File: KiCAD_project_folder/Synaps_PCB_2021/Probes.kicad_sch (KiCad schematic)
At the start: 2 parts, among them J3 Conn_01x20_MountingPin, U2 CD74HC4067M

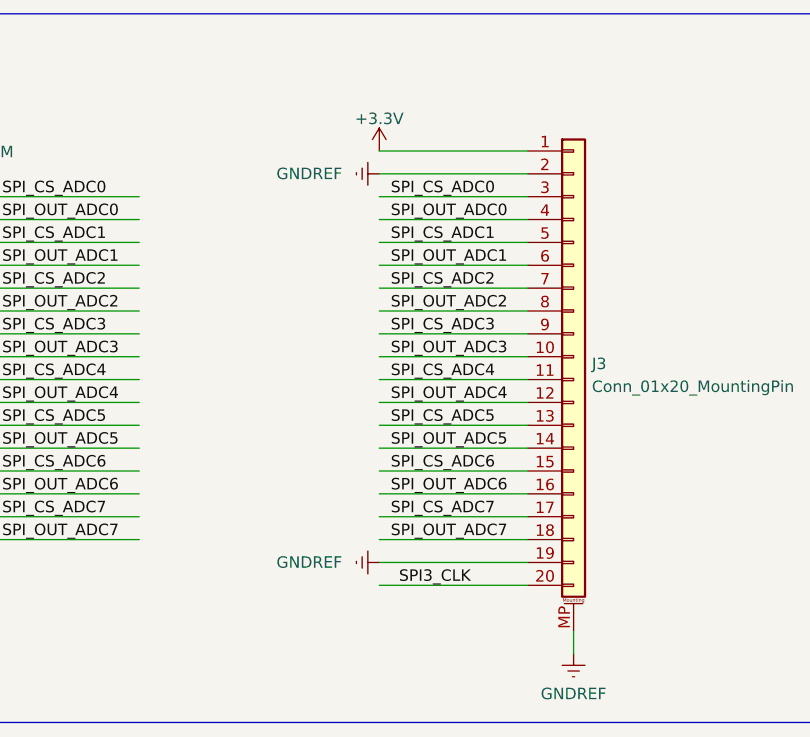
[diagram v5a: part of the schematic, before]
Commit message: Fixed missing connections + plus added rough BOM
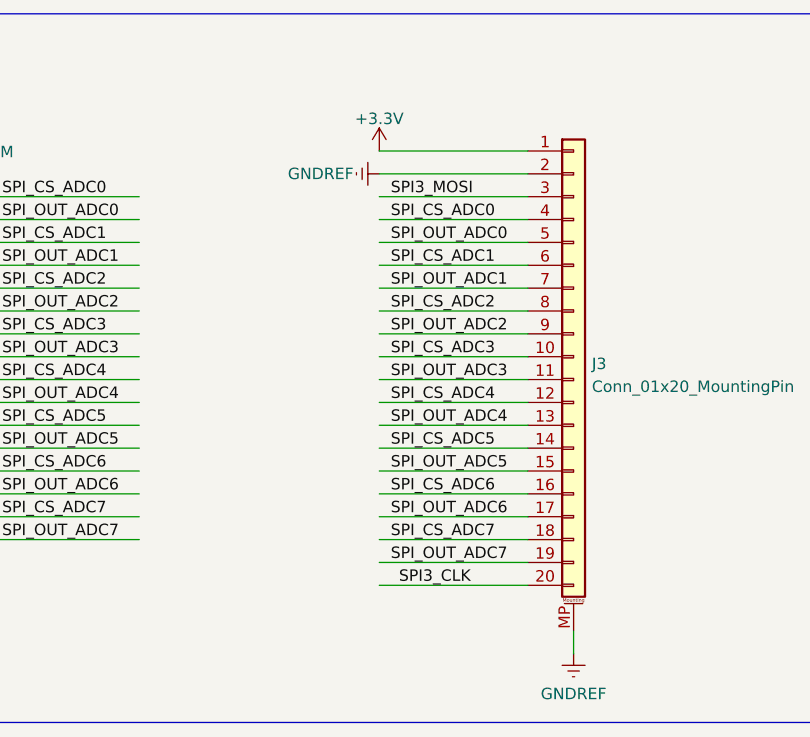
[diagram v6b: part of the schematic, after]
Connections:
- net GNDREF: no longer J3.19 (Pin_19)
- net SPI3_MOSI: now also J3.3 (Pin_3)
- net SPI_CS_ADC0: now also J3.4 (Pin_4); no longer J3.3 (Pin_3)
- net SPI_CS_ADC1: now also J3.6 (Pin_6); no longer J3.5 (Pin_5)
- net SPI_CS_ADC2: now also J3.8 (Pin_8); no longer J3.7 (Pin_7)
- net SPI_CS_ADC3: now also J3.10 (Pin_10); no longer J3.9 (Pin_9)
- net SPI_CS_ADC4: now also J3.12 (Pin_12); no longer J3.11 (Pin_11)
- net SPI_CS_ADC5: now also J3.14 (Pin_14); no longer J3.13 (Pin_13)
- net SPI_CS_ADC6: now also J3.16 (Pin_16); no longer J3.15 (Pin_15)
- net SPI_CS_ADC7: now also J3.18 (Pin_18); no longer J3.17 (Pin_17)
- net SPI_OUT_ADC0: now also J3.5 (Pin_5); no longer J3.4 (Pin_4)
- net SPI_OUT_ADC1: now also J3.7 (Pin_7); no longer J3.6 (Pin_6)
- net SPI_OUT_ADC2: now also J3.9 (Pin_9); no longer J3.8 (Pin_8)
- net SPI_OUT_ADC3: now also J3.11 (Pin_11); no longer J3.10 (Pin_10)
- net SPI_OUT_ADC4: now also J3.13 (Pin_13); no longer J3.12 (Pin_12)
- net SPI_OUT_ADC5: now also J3.15 (Pin_15); no longer J3.14 (Pin_14)
- net SPI_OUT_ADC6: now also J3.17 (Pin_17); no longer J3.16 (Pin_16)
- net SPI_OUT_ADC7: now also J3.19 (Pin_19); no longer J3.18 (Pin_18)
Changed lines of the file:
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@@
     (effects (font (size 1.27 1.27)) (justify left bottom))
   )
-  (label "SPI_OUT_ADC7" (at 199.39 81.28 0)
-    (effects (font (size 1.27 1.27)) (justify left bottom))
-  )
-  (label "SPI_CS_ADC7" (at 199.39 78.74 0)
+  (label "SPI_OUT_ADC7" (at 199.39 83.82 0)
+    (effects (font (size 1.27 1.27)) (justify left bottom))
+  )
+  (label "SPI_CS_ADC7" (at 199.39 81.28 0)
     (effects (font (size 1.27 1.27)) (justify left bottom))
   )
@@
     (effects (font (size 1.27 1.27)) (justify left bottom))
   )
-  (label "SPI_OUT_ADC2" (at 199.39 55.88 0)
-    (effects (font (size 1.27 1.27)) (justify left bottom))
-  )
-  (label "SPI_OUT_ADC3" (at 199.39 60.96 0)
-    (effects (font (size 1.27 1.27)) (justify left bottom))
-  )
-  (label "SPI_CS_ADC6" (at 199.39 73.66 0)
+  (label "SPI3_MOSI" (at 199.39 43.18 0)
+    (effects (font (size 1.27 1.27)) (justify left bottom))
+  )
+  (label "SPI_OUT_ADC2" (at 199.39 58.42 0)
+    (effects (font (size 1.27 1.27)) (justify left bottom))
+  )
+  (label "SPI_OUT_ADC3" (at 199.39 63.5 0)
+    (effects (font (size 1.27 1.27)) (justify left bottom))
+  )
+  (label "SPI_CS_ADC6" (at 199.39 76.2 0)
     (effects (font (size 1.27 1.27)) (justify left bottom))
   )
@@
     (effects (font (size 1.27 1.27)) (justify right bottom))
   )
-  (label "SPI_CS_ADC3" (at 199.39 58.42 0)
+  (label "SPI_CS_ADC3" (at 199.39 60.96 0)
     (effects (font (size 1.27 1.27)) (justify left bottom))
   )
@@
     (effects (font (size 1.27 1.27)) (justify left bottom))
   )
-  (label "SPI_CS_ADC4" (at 199.39 63.5 0)
+  (label "SPI_CS_ADC4" (at 199.39 66.04 0)
     (effects (font (size 1.27 1.27)) (justify left bottom))
   )
@@
     (effects (font (size 1.27 1.27)) (justify left bottom))
   )
-  (label "SPI_CS_ADC0" (at 199.39 43.18 0)
-    (effects (font (size 1.27 1.27)) (justify left bottom))
-  )
-  (label "SPI_OUT_ADC0" (at 199.39 45.72 0)
-    (effects (font (size 1.27 1.27)) (justify left bottom))
-  )
-  (label "SPI_CS_ADC1" (at 199.39 48.26 0)
-    (effects (font (size 1.27 1.27)) (justify left bottom))
-  )
-  (label "SPI_CS_ADC2" (at 199.39 53.34 0)
-    (effects (font (size 1.27 1.27)) (justify left bottom))
-  )
-  (label "SPI_CS_ADC5" (at 199.39 68.58 0)
+  (label "SPI_CS_ADC0" (at 199.39 45.72 0)
+    (effects (font (size 1.27 1.27)) (justify left bottom))
+  )
+  (label "SPI_OUT_ADC0" (at 199.39 48.26 0)
+    (effects (font (size 1.27 1.27)) (justify left bottom))
+  )
+  (label "SPI_CS_ADC1" (at 199.39 50.8 0)
+    (effects (font (size 1.27 1.27)) (justify left bottom))
+  )
+  (label "SPI_CS_ADC2" (at 199.39 55.88 0)
+    (effects (font (size 1.27 1.27)) (justify left bottom))
+  )
+  (label "SPI_CS_ADC5" (at 199.39 71.12 0)
     (effects (font (size 1.27 1.27)) (justify left bottom))
   )
@@
     (effects (font (size 1.27 1.27)) (justify right bottom))
   )
-  (label "SPI_OUT_ADC6" (at 199.39 76.2 0)
-    (effects (font (size 1.27 1.27)) (justify left bottom))
-  )
-  (label "SPI_OUT_ADC1" (at 199.39 50.8 0)
-    (effects (font (size 1.27 1.27)) (justify left bottom))
-  )
-  (label "SPI_OUT_ADC5" (at 199.39 71.12 0)
+  (label "SPI_OUT_ADC6" (at 199.39 78.74 0)
+    (effects (font (size 1.27 1.27)) (justify left bottom))
+  )
+  (label "SPI_OUT_ADC1" (at 199.39 53.34 0)
+    (effects (font (size 1.27 1.27)) (justify left bottom))
+  )
+  (label "SPI_OUT_ADC5" (at 199.39 73.66 0)
     (effects (font (size 1.27 1.27)) (justify left bottom))
   )
@@
     (effects (font (size 1.27 1.27)) (justify right bottom))
   )
-  (label "SPI_OUT_ADC4" (at 199.39 66.04 0)
+  (label "SPI_OUT_ADC4" (at 199.39 68.58 0)
     (effects (font (size 1.27 1.27)) (justify left bottom))
   )
@@
     (pin "MP")
   )
+  (symbol (lib_id "power:GNDREF") (at 198.12 40.64 270) (unit 1)
+    (in_bom yes) (on_board yes)
+    (property "Reference" "#PWR0101" (id 0) (at 191.77 40.64 0)
+      (effects (font (size 1.27 1.27)) hide)
+    )
+    (property "Value" "GNDREF" (id 1) (at 187.96 40.64 90)
+      (effects (font (size 1.27 1.27)) (justify left))
+    )
+    (property "Footprint" "" (id 2) (at 198.12 40.64 0)
+      (effects (font (size 1.27 1.27)) hide)
+    )
+    (property "Datasheet" "" (id 3) (at 198.12 40.64 0)
+      (effects (font (size 1.27 1.27)) hide)
+    )
+    (pin "1")
+  )
   (symbol (lib_id "power:+3.3V") (at 198.12 38.1 0) (unit 1)
     (in_bom yes) (on_board yes) (fields_autoplaced)
@@
       (effects (font (size 1.27 1.27)) hide)
     )
-    (pin "1")
-  )
-  (symbol (lib_id "power:GNDREF") (at 198.12 83.82 270) (unit 1)
-    (in_bom yes) (on_board yes)
-    (property "Reference" "#PWR050" (id 0) (at 191.77 83.82 0)
-      (effects (font (size 1.27 1.27)) hide)
-    )
-    (property "Value" "GNDREF" (id 1) (at 186.69 83.82 90)
-      (effects (font (size 1.27 1.27)) (justify left))
-    )
-    (property "Footprint" "" (id 2) (at 198.12 83.82 0)
-      (effects (font (size 1.27 1.27)) hide)
-    )
-    (property "Datasheet" "" (id 3) (at 198.12 83.82 0)
-      (effects (font (size 1.27 1.27)) hide)
-    )
-    (pin "1")
-  )
-  (symbol (lib_id "power:GNDREF") (at 198.12 40.64 270) (unit 1)
-    (in_bom yes) (on_board yes)
-    (property "Reference" "#PWR049" (id 0) (at 191.77 40.64 0)
-      (effects (font (size 1.27 1.27)) hide)
-    )
-    (property "Value" "GNDREF" (id 1) (at 186.69 40.64 90)
-      (effects (font (size 1.27 1.27)) (justify left))
-    )
-    (property "Footprint" "" (id 2) (at 198.12 40.64 0)
-      (effects (font (size 1.27 1.27)) hide)
-    )
-    (property "Datasheet" "" (id 3) (at 198.12 40.64 0)
-      (effects (font (size 1.27 1.27)) hide)
-    )

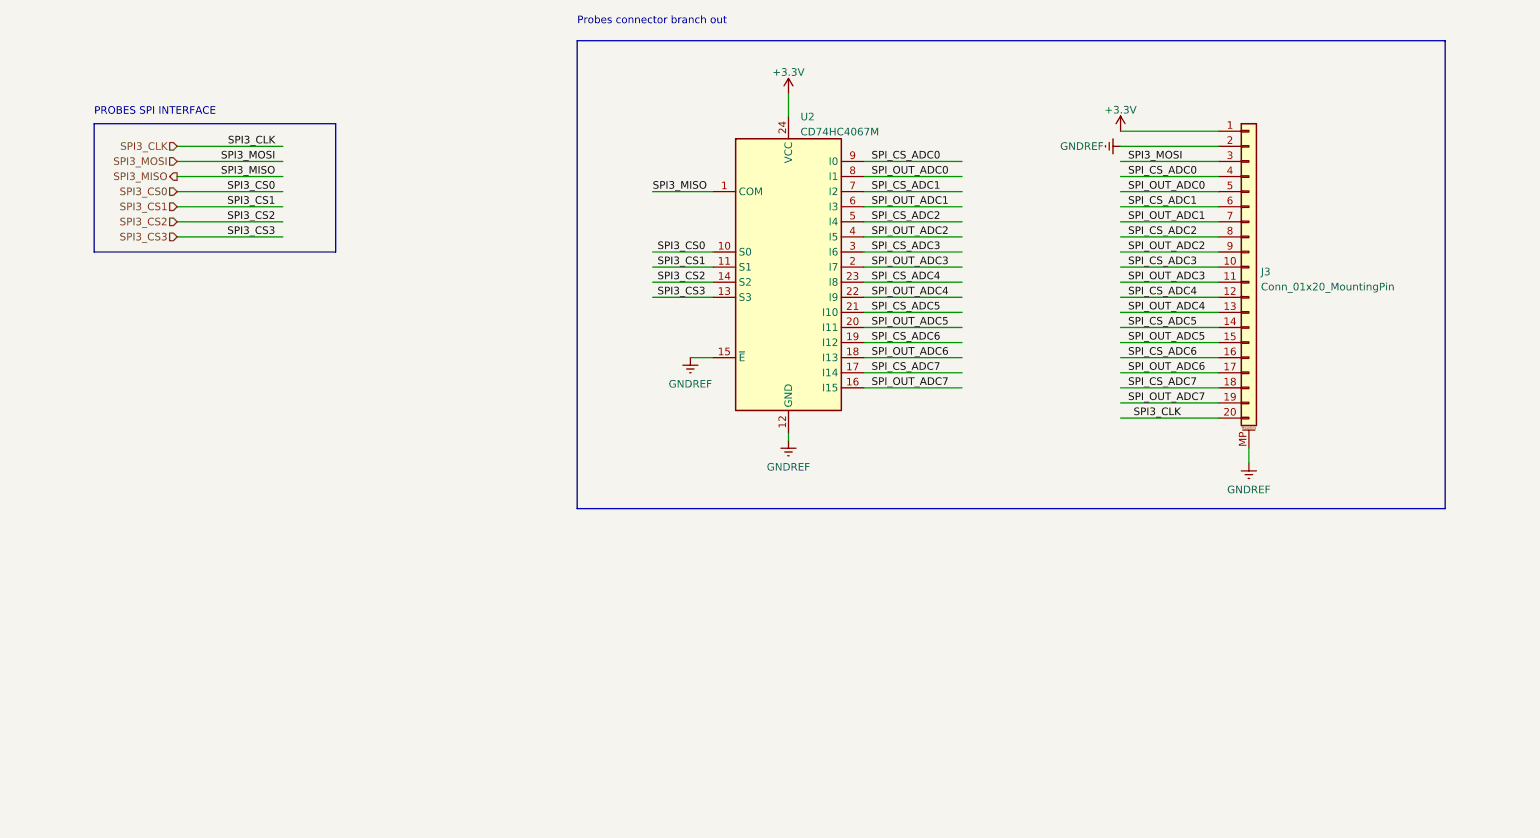
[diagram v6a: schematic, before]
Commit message: Updated BOM and power circuit has to be redone because of missing parts
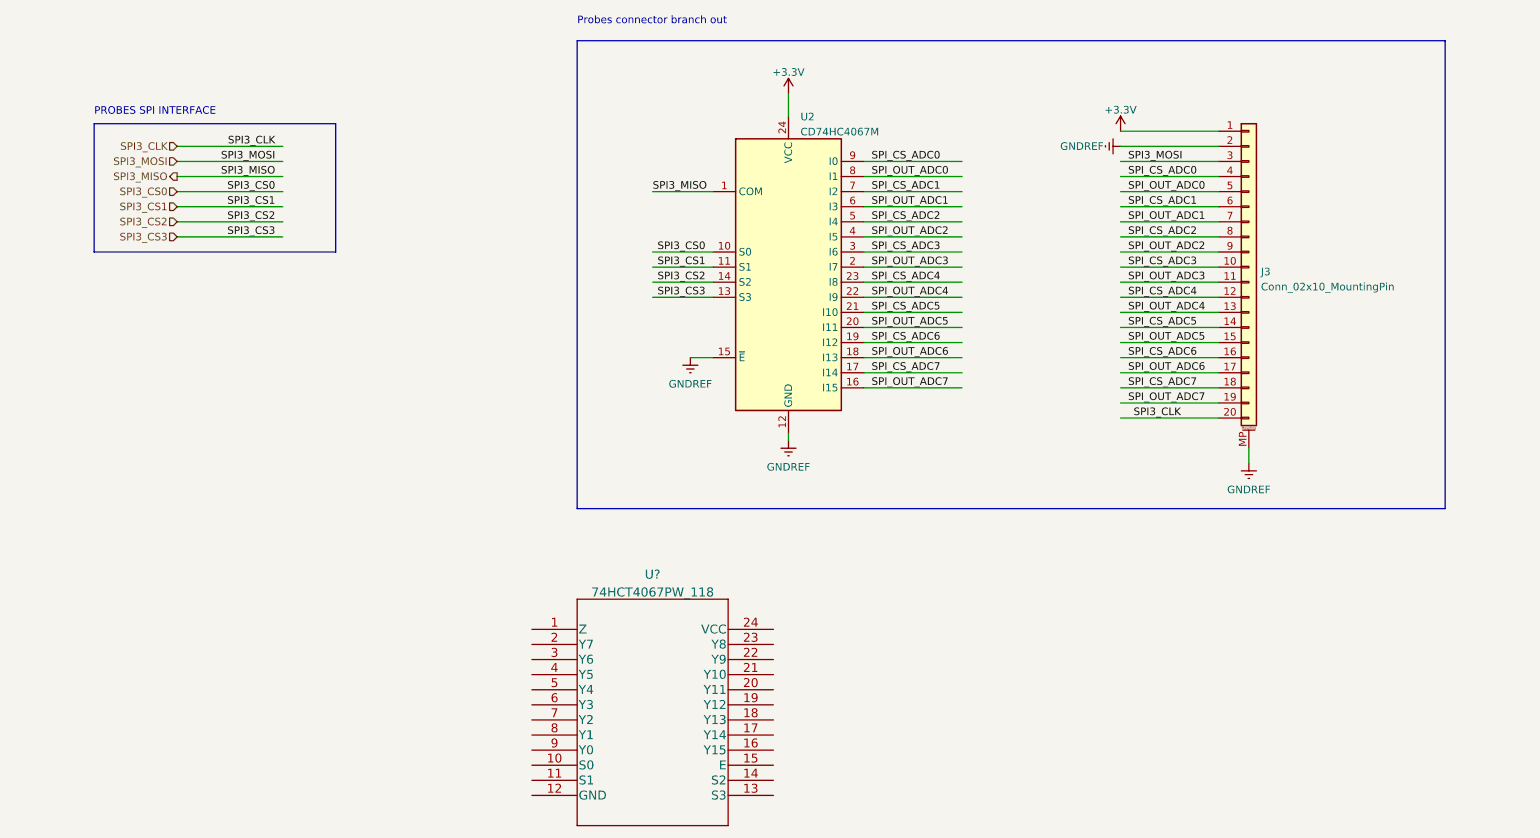
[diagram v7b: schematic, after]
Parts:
- added U?: 74HCT4067PW_118, 74HCT4067PW-118:74HCT4067PW_118, symbol 74HCT4067PW-118:74HCT4067PW_118
- J3: value Conn_01x20_MountingPin -> Conn_02x10_MountingPin; footprint Connector_PinHeader_2.00mm:PinHeader_1x20_P2.00mm_Vertical -> Connector_PinHeader_2.54mm:PinHeader_2x10_P2.54mm_Vertical_SMD; MPN (none) -> 3020-20-0300-00; Supplier Link (none) -> https://www.digikey.ca/en/products/detail/cnc-tech/3020-20-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
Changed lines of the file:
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@@
       (effects (font (size 1.27 1.27)) (justify left))
     )
-    (property "Value" "Conn_01x20_MountingPin" (id 1) (at 221.742 64.2878 0)
+    (property "Value" "Conn_02x10_MountingPin" (id 1) (at 221.742 64.2878 0)
       (effects (font (size 1.27 1.27)) (justify left))
     )
-    (property "Footprint" "Connector_PinHeader_2.00mm:PinHeader_1x20_P2.00mm_Vertical" (id 2) (at 219.71 60.96 0)
+    (property "Footprint" "Connector_PinHeader_2.54mm:PinHeader_2x10_P2.54mm_Vertical_SMD" (id 2) (at 219.71 60.96 0)
       (effects (font (size 1.27 1.27)) hide)
     )
-    (property "Datasheet" "~" (id 3) (at 219.71 60.96 0)
+    (property "Datasheet" "https://www.cnctech.us/pdfs/3020-XX-0300-00%20(9T).pdf" (id 3) (at 219.71 60.96 0)
+      (effects (font (size 1.27 1.27)) hide)
+    )
+    (property "MPN" "3020-20-0300-00" (id 4) (at 219.71 60.96 0)
+      (effects (font (size 1.27 1.27)) hide)
+    )
+    (property "Supplier Link" "https://www.digikey.ca/en/products/detail/cnc-tech/3020-20-0300-00/3441742" (id 5) (at 219.71 60.96 0)
       (effects (font (size 1.27 1.27)) hide)
     )
@@
     (pin "1")
   )
+  (symbol (lib_id "74HCT4067PW-118:74HCT4067PW_118") (at 99.06 121.92 0) (unit 1)
+    (in_bom yes) (on_board yes) (fields_autoplaced)
+    (property "Reference" "U?" (id 0) (at 119.38 112.6924 0)
+      (effects (font (size 1.524 1.524)))
+    )
+    (property "Value" "74HCT4067PW_118" (id 1) (at 119.38 115.6858 0)
+      (effects (font (size 1.524 1.524)))
+    )
+    (property "Footprint" "74HCT4067PW-118:74HCT4067PW_118" (id 2) (at 119.38 115.824 0)
+      (effects (font (size 1.524 1.524)) hide)
+    )
+    (property "Datasheet" "https://assets.nexperia.com/documents/data-sheet/74HC_HCT4067.pdf" (id 3) (at 99.06 121.92 0)
+      (effects (font (size 1.524 1.524)) hide)
+    )
+    (property "MPN" "74HCT4067PW,118" (id 4) (at 99.06 121.92 0)
+      (effects (font (size 1.27 1.27)) hide)
+    )
+    (property "Supplier Link" "https://www.digikey.ca/en/products/detail/nexperia-usa-inc/74HCT4067PW-118/1230918" (id 5) (at 99.06 121.92 0)
+      (effects (font (size 1.27 1.27)) hide)
+    )
+    (pin "1")
+    (pin "10")
+    (pin "11")
+    (pin "12")
+    (pin "13")
+    (pin "14")
+    (pin "15")
+    (pin "16")
+    (pin "17")
+    (pin "18")
+    (pin "19")
+    (pin "2")
+    (pin "20")
+    (pin "21")
+    (pin "22")
+    (pin "23")
+    (pin "24")
+    (pin "3")
+    (pin "4")
+    (pin "5")
+    (pin "6")
+    (pin "7")
+    (pin "8")
+    (pin "9")
+  )
   (symbol (lib_id "power:GNDREF") (at 142.24 90.17 0) (unit 1)

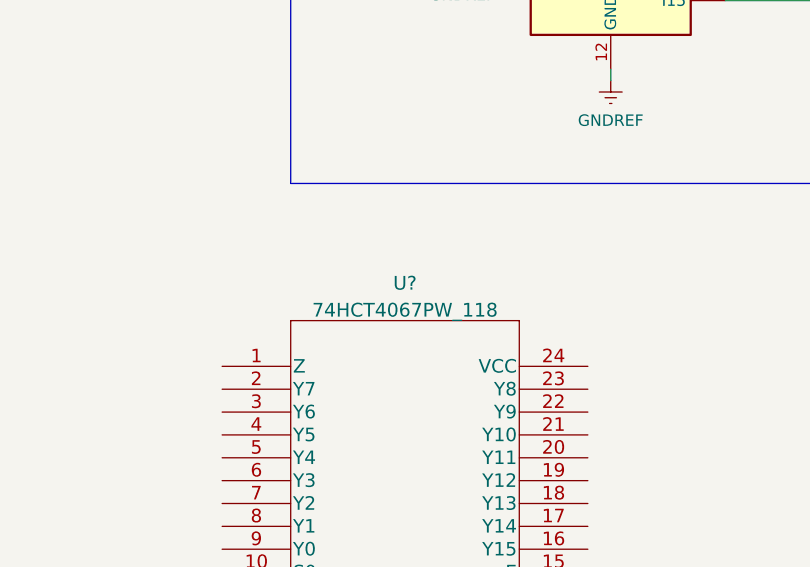
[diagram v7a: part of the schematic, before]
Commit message: updated libraries and added parts for TPS25741
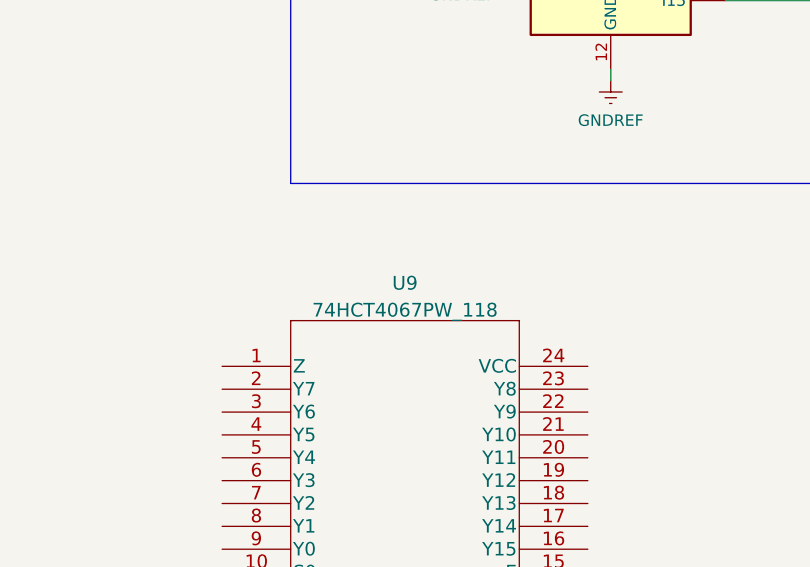
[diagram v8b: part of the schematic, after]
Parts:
- gave numbers to parts that had none: 1
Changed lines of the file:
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@@
   (symbol (lib_id "74HCT4067PW-118:74HCT4067PW_118") (at 99.06 121.92 0) (unit 1)
     (in_bom yes) (on_board yes) (fields_autoplaced)
-    (property "Reference" "U?" (id 0) (at 119.38 112.6924 0)
+    (property "Reference" "U9" (id 0) (at 119.38 112.6924 0)
       (effects (font (size 1.524 1.524)))
     )
